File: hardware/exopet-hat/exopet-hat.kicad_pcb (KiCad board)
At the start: 2 copper layers, 65 x 56 mm, 48 parts, among them J1 BarrelJack_CUI_PJ-102AH_Horiz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, J10 TerminalBlock_Phoenix_MKDS-1,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, J11 TerminalBlock_Phoenix_MKDS-1,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, J2 SolderWire-1.5sqmm_1x02_P6mm_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, J3 PinSocket_2x20_P2.54mm_Vertic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, J4 Jack_3.5mm_CUI_SJ-3523-SMT_Ho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, J8 TerminalBlock_Phoenix_MKDS-1,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, J9 TerminalBlock_Phoenix_MKDS-1,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, K1 Relay_SPDT_Omron-G5LE-1, K2 Relay_SPDT_Omron-G5LE-1, K3 Relay_SPDT_Omron-G5LE-1, K4 Relay_SPDT_Omron-G5LE-1, Q1 TO-252-2, U2 SOIC-16_3.9x9.9mm_P1.27mm, U4 SOIC-8_3.9x4.9mm_P1.27mm, U5 D_SOD-323

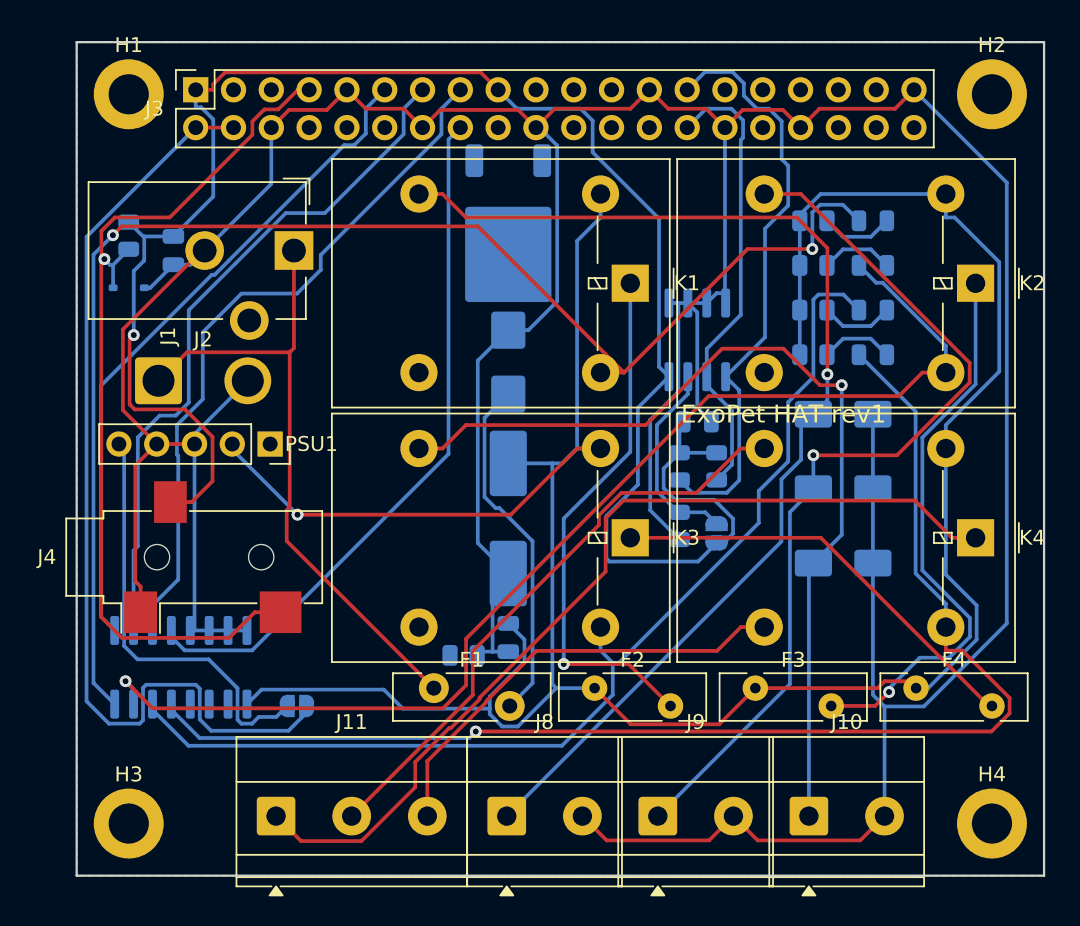
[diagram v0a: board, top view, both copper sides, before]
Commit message: Regroup HAT terminals per function; add float switch inputs
- Front edge: CH1/CH2/CH3 switched-12V blocks separated, CH4 dry
  contact last; left edge: FLOAT1, FLOAT2, TEMP sensor stack
- Temperature input is now a 3-pos screw terminal (TRS jack and JST
  both removed) - bare probe wires screw straight in
- Added the missing float switch inputs: GPIO16 (tank, matches hub
  code) and GPIO12 (sump spec), each with 10k pull-up, 1k series
  resistor, and 100nF filter
- All terminals now Phoenix PT-1,5 3.5mm; J2 aux 12V input removed
  (barrel jack sole input)
- Rerouted: 112 connections, 0 unrouted; DRC fully clean (0 violations)

Co-Authored-By: Claude Fable 5 <noreply@anthropic.com>
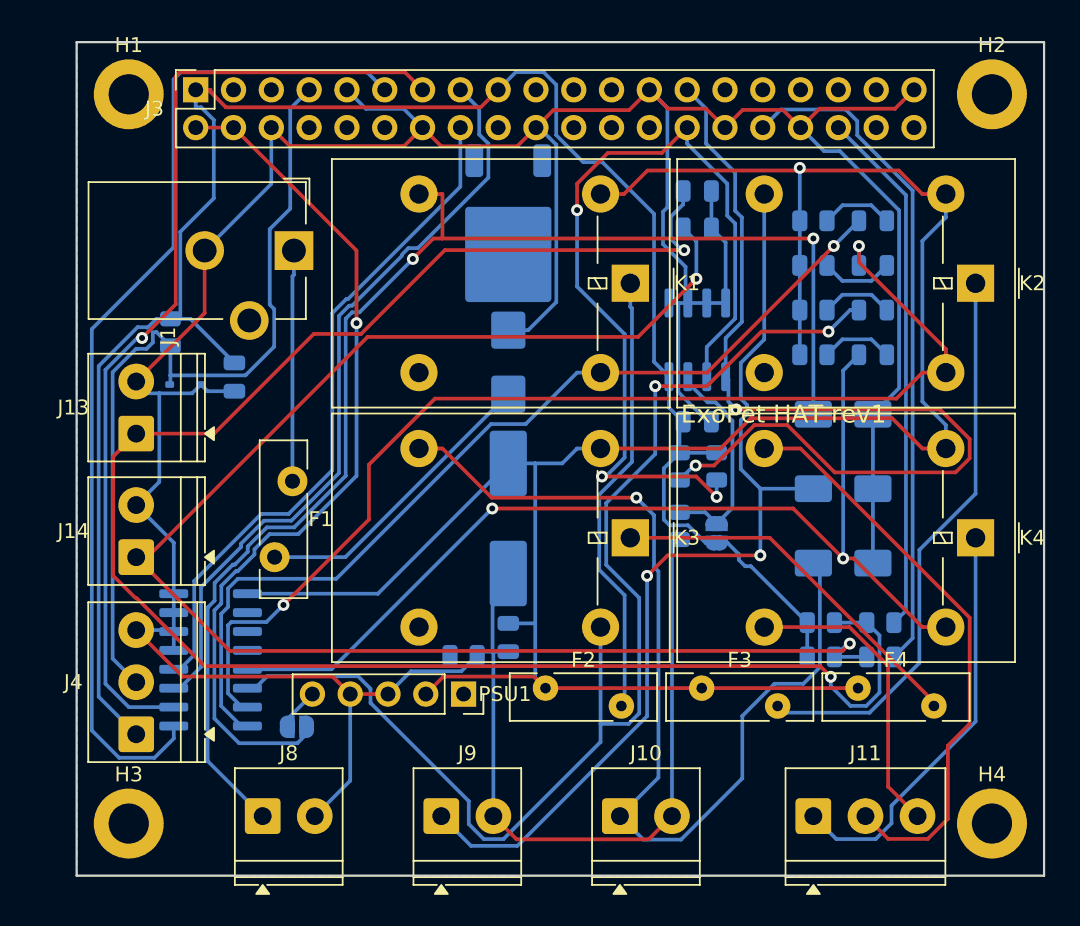
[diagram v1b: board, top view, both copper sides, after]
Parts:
- removed J2: SolderWire-1.5sqmm_1x02_P6mm_D1.7mm_OD3mm, Connector_Wire:SolderWire-1.5sqmm_1x02_P6mm_D1.7mm_OD3mm
- added C5: C_0805_2012Metric, Capacitor_SMD:C_0805_2012Metric, B.Cu at (41.7, 10.0)
- added C6: C_0805_2012Metric, Capacitor_SMD:C_0805_2012Metric, B.Cu at (41.7, 12.5)
- added J13: TerminalBlock_Phoenix_PT-1,5-2-3.5-H_1x02_P3.50mm_Horizontal, TerminalBlock_Phoenix:TerminalBlock_Phoenix_PT-1,5-2-3.5-H_1x02_P3.50mm_Horizontal, F.Cu at (4.00, 26.3)
- added J14: TerminalBlock_Phoenix_PT-1,5-2-3.5-H_1x02_P3.50mm_Horizontal, TerminalBlock_Phoenix:TerminalBlock_Phoenix_PT-1,5-2-3.5-H_1x02_P3.50mm_Horizontal, F.Cu at (4.00, 34.6)
- added R10: R_0805_2012Metric, Resistor_SMD:R_0805_2012Metric, B.Cu at (50.0, 39.0)
- added R11: R_0805_2012Metric, Resistor_SMD:R_0805_2012Metric, B.Cu at (50.0, 41.3)
- added R12: R_0805_2012Metric, Resistor_SMD:R_0805_2012Metric, B.Cu at (54.0, 39.0)
- added R13: R_0805_2012Metric, Resistor_SMD:R_0805_2012Metric, B.Cu at (54.0, 41.3)
- J10, J8, J9: value TerminalBlock_Phoenix_MKDS-1,5-2-5.08_1x02_P5.08mm_Horizontal -> TerminalBlock_Phoenix_PT-1,5-2-3.5-H_1x02_P3.50mm_Horizontal; footprint TerminalBlock_Phoenix:TerminalBlock_Phoenix_MKDS-1,5-2-5.08_1x02_P5.08mm_Horizontal -> TerminalBlock_Phoenix:TerminalBlock_Phoenix_PT-1,5-2-3.5-H_1x02_P3.50mm_Horizontal
- J11: value TerminalBlock_Phoenix_MKDS-1,5-3-5.08_1x03_P5.08mm_Horizontal -> TerminalBlock_Phoenix_PT-1,5-3-3.5-H_1x03_P3.50mm_Horizontal; footprint TerminalBlock_Phoenix:TerminalBlock_Phoenix_MKDS-1,5-3-5.08_1x03_P5.08mm_Horizontal -> TerminalBlock_Phoenix:TerminalBlock_Phoenix_PT-1,5-3-3.5-H_1x03_P3.50mm_Horizontal
- J4: value Jack_3.5mm_CUI_SJ-3523-SMT_Horizontal -> TerminalBlock_Phoenix_PT-1,5-3-3.5-H_1x03_P3.50mm_Horizontal; footprint Connector_Audio:Jack_3.5mm_CUI_SJ-3523-SMT_Horizontal -> TerminalBlock_Phoenix:TerminalBlock_Phoenix_PT-1,5-3-3.5-H_1x03_P3.50mm_Horizontal
- moved J11 36.1 mm to (49.5, 52.0)
- moved PSU1 21.2 mm to (26.0, 43.8)
- moved F1 16.8 mm to (14.5, 29.5), turned to -90 degrees
- moved J8 16.4 mm to (12.5, 52.0)
- moved J9 14.5 mm to (24.5, 52.0)
- moved J10 12.7 mm to (36.5, 52.0)
- moved J4 12.5 mm to (4.00, 46.5)
- moved C3 9.44 mm to (10.6, 22.5)
- moved U5 7.53 mm to (7.30, 23.0)
- moved R2 7.08 mm to (6.30, 19.5)
- moved F4 3.90 mm to (52.5, 43.4)
- moved F3 3.60 mm to (42.0, 43.4)
- moved F2 3.30 mm to (31.5, 43.4)
- moved U2 2.06 mm to (9.00, 41.5), turned to 0 degrees
- moved JP1 1.40 mm to (14.8, 46.0)
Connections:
- J3 pad 32: unconnected-(J3-PWM0/GPIO12-Pad32) -> FLOAT2_GPIO
- J3 pad 36: unconnected-(J3-GPIO16-Pad36) -> FLOAT1_GPIO
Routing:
- net FLOAT1_SW: track 0.00 -> 119.9 mm, vias 0 -> 2
- net FLOAT2_SW: track 0.00 -> 103.5 mm, vias 0 -> 2
- net FLOAT2_GPIO: track 0.00 -> 45.2 mm
- net FLOAT1_GPIO: track 0.00 -> 35.5 mm
- net CH4_COM: track 61.4 -> 27.8 mm
- net RLY1_DRV: track 95.2 -> 63.0 mm, vias 2 -> 1
- net +12V: track 184.9 -> 155.3 mm
- net EEPROM_SCL: track 30.9 -> 59.0 mm, vias 0 -> 3
- net +12V_IN: track 43.3 -> 15.5 mm
- net +5V_BUCK: track 28.6 -> 2.90 mm
- net GND: track 302.2 -> 277.2 mm
- net EEPROM_SDA: track 39.8 -> 64.3 mm, vias 0 -> 2
- net GPIO17: track 45.1 -> 68.5 mm
- net GPIO27: track 46.5 -> 65.4 mm, vias 0 -> 1
- net RLY4_DRV: track 87.1 -> 68.8 mm, vias 1 -> 2
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
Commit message: Fix GPIO socket to bottom side per official HAT template; refresh fab package
Critical fix caught before ordering: the 2x20 socket body was generated
on the top side and off-position — physically unable to mate with a Pi.
Now matches KiCad's official RaspberryPi-HAT template exactly (B.Cu,
pin 1 at 8.37,4.77 from the hole datum) with tools/verify_j3.py as a
permanent regression assert.

Also: C1 changed to low-profile 6.3x7.7mm (330uF) for under-HAT
clearance; verified in-stock LCSC codes baked into the assembly BOM
(PC104 stacking socket C35165, CUI PJ-102A C20518877, KF350 terminals,
RGEF500/RXEF110 fuses, PESD5V0S1BA ESD diode, 1x5 socket C50950).
Rerouted, DRC clean (0 errors), renders and fab files regenerated.

Co-Authored-By: Claude Fable 5 <noreply@anthropic.com>
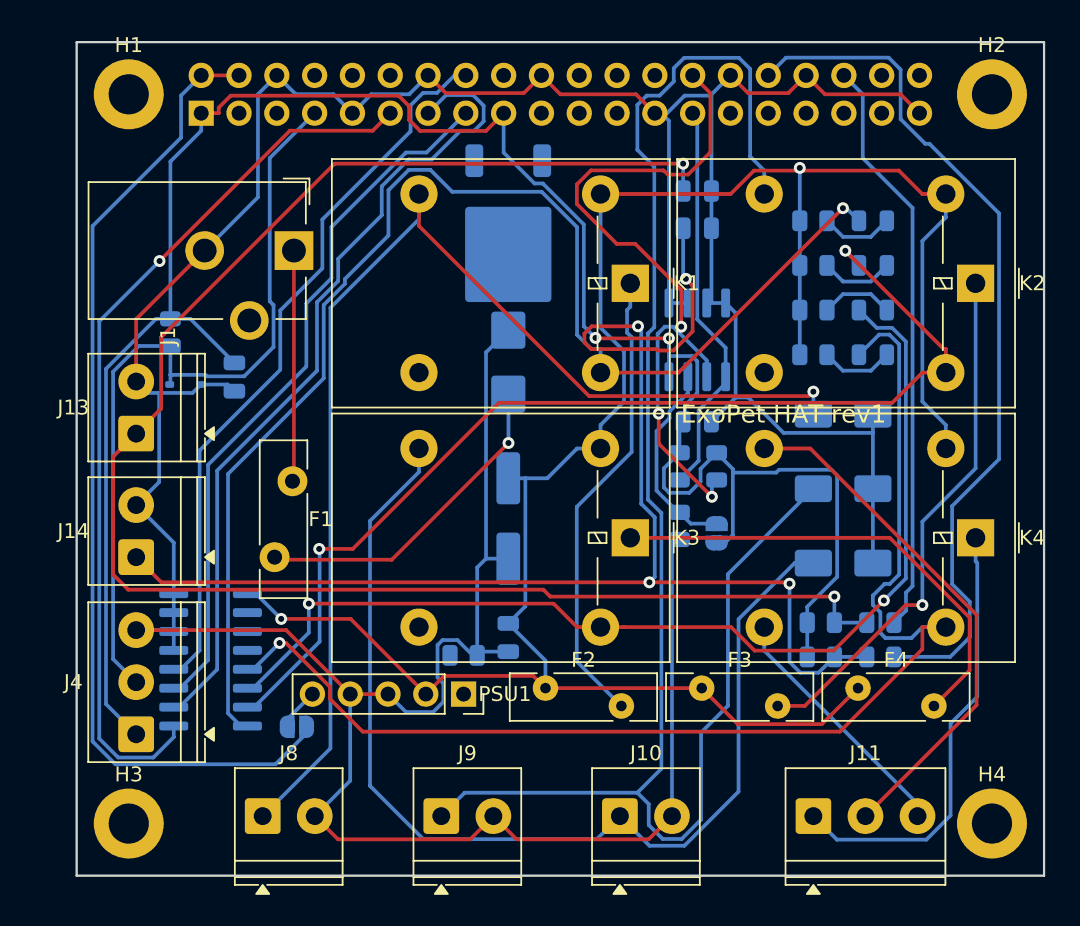
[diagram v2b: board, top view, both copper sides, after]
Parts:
- C1: value CP_Elec_8x10.5 -> CP_Elec_6.3x7.7; footprint Capacitor_SMD:CP_Elec_8x10.5 -> Capacitor_SMD:CP_Elec_6.3x7.7
- J3: moved to B.Cu
- moved J3 1.61 mm to (8.37, 4.77), turned to -90 degrees
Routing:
- net CH2_OUT: track 65.3 -> 112.5 mm, vias 2 -> 0
- net EEPROM_SDA: track 64.3 -> 26.8 mm, vias 2 -> 0
- net RLY1_DRV: track 63.0 -> 89.2 mm
- net RLY4_DRV: track 68.8 -> 83.3 mm, vias 2 -> 1
- net FLOAT2_GPIO: track 45.2 -> 58.2 mm
- net RLY3_DRV: track 83.4 -> 71.0 mm
- net +3V3: track 132.1 -> 144.1 mm, vias 0 -> 2
- net +12V: track 155.3 -> 143.4 mm, vias 1 -> 2
- net EEPROM_SCL: track 59.0 -> 48.6 mm
- net FLOAT2_SW: track 103.5 -> 93.3 mm, vias 2 -> 4
- net GPIO27: track 65.4 -> 55.2 mm, vias 1 -> 0
- net CH1_OUT: track 90.0 -> 81.2 mm, vias 2 -> 1
- net GPIO17: track 68.5 -> 60.2 mm, vias 0 -> 1
- net +5V: track 58.4 -> 66.6 mm, vias 1 -> 0
- net FLOAT1_SW: track 119.9 -> 112.0 mm
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
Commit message: HAT rev 2: schematic + placement — integrated buck, D1 fix, top LEDs, TPs
TPS54302 synchronous buck replaces the Pololu socket (datasheet-derived
5.06V design; 5A TPS54531 didn't fit the relay-pad corridors). D1 nets
corrected + bidirectional SMBJ16CA. Channel LEDs move to the top
between terminal blocks; 12V/5V rail LEDs + 4 test points top-left.
Terminal +/- and COM/NO/NC silk, jack polarity text, PTC fuse drills
enlarged to 1.1mm. New check_polarity.py lints every polarized part
from the netlist; check_placement.py now also catches SMD-vs-THT-pad
collisions (found two latent rev-1 near-misses). ERC clean, polarity
lint clean, placement clean, J3 template-verified.

Co-Authored-By: Claude Fable 5 <noreply@anthropic.com>
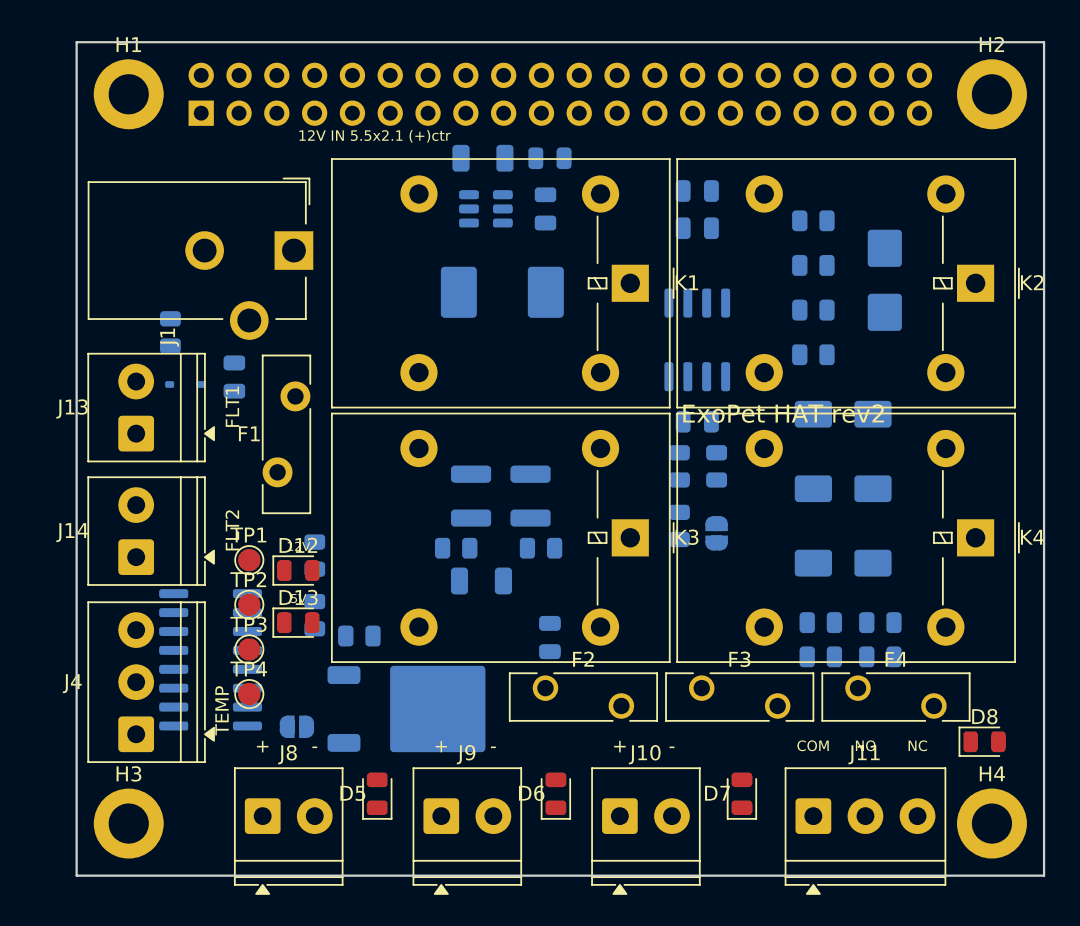
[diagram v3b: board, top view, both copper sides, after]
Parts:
- removed C1: CP_Elec_6.3x7.7, Capacitor_SMD:CP_Elec_6.3x7.7
- removed PSU1: PinSocket_1x05_P2.54mm_Vertical, Connector_PinSocket_2.54mm:PinSocket_1x05_P2.54mm_Vertical
- added C10: C_0805_2012Metric, Capacitor_SMD:C_0805_2012Metric, B.Cu at (31.8, 7.80)
- added C11: C_1210_3225Metric, Capacitor_SMD:C_1210_3225Metric, B.Cu at (26.5, 30.5)
- added C12: C_1210_3225Metric, Capacitor_SMD:C_1210_3225Metric, B.Cu at (30.5, 30.5)
- added C16: C_1206_3216Metric, Capacitor_SMD:C_1206_3216Metric, B.Cu at (27.2, 36.2)
- added C7: C_0805_2012Metric, Capacitor_SMD:C_0805_2012Metric, B.Cu at (31.5, 11.2)
- added C8: C_1206_3216Metric, Capacitor_SMD:C_1206_3216Metric, B.Cu at (27.3, 7.80)
- added D12: LED_0805_2012Metric, LED_SMD:LED_0805_2012Metric, F.Cu at (14.9, 35.5)
- added D13: LED_0805_2012Metric, LED_SMD:LED_0805_2012Metric, F.Cu at (14.9, 39.0)
- added L1: L_Vishay_IHLP-2525, Inductor_SMD:L_Vishay_IHLP-2525, B.Cu at (28.6, 16.8)
- added R16: R_0805_2012Metric, Resistor_SMD:R_0805_2012Metric, B.Cu at (25.5, 34.0)
- added R17: R_0805_2012Metric, Resistor_SMD:R_0805_2012Metric, B.Cu at (31.2, 34.0)
- added R19: R_0805_2012Metric, Resistor_SMD:R_0805_2012Metric, B.Cu at (16.0, 34.5)
- added R20: R_0805_2012Metric, Resistor_SMD:R_0805_2012Metric, B.Cu at (16.0, 38.5)
- added TP1: TestPoint_Pad_D1.5mm, TestPoint:TestPoint_Pad_D1.5mm, F.Cu at (11.6, 34.8)
- added TP2: TestPoint_Pad_D1.5mm, TestPoint:TestPoint_Pad_D1.5mm, F.Cu at (11.6, 37.8)
- added TP3: TestPoint_Pad_D1.5mm, TestPoint:TestPoint_Pad_D1.5mm, F.Cu at (11.6, 40.8)
- added TP4: TestPoint_Pad_D1.5mm, TestPoint:TestPoint_Pad_D1.5mm, F.Cu at (11.6, 43.8)
- added U6: SOT-23-6, Package_TO_SOT_SMD:SOT-23-6, B.Cu at (27.5, 11.2)
- D5, D6, D7, D8: moved to F.Cu
- moved D5 50.9 mm to (20.2, 50.5), turned to 90 degrees
- moved D6 41.4 mm to (32.2, 50.5), turned to 90 degrees
- moved D7 33.7 mm to (44.7, 50.5), turned to 90 degrees
- moved Q1 32.4 mm to (23.0, 44.8), turned to 0 degrees
- moved D8 27.1 mm to (61.0, 47.0)
- moved D1 25.9 mm to (54.3, 16.0)
- moved R1 7.12 mm to (19.0, 39.9)
- moved C2 2.80 mm to (31.8, 40.0)
- moved F1 1.17 mm to (13.5, 28.9), turned to 90 degrees
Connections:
- D1 pad 1: GND -> +12V_F
- D1 pad 2: +12V_F -> GND
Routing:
- net GND: track 273.5 -> 0.00 mm
- net +3V3: track 144.1 -> 0.00 mm, vias 2 -> 0
- net +12V: track 143.4 -> 0.00 mm, vias 2 -> 0
- net CH2_OUT: track 112.5 -> 0.00 mm
- net FLOAT1_SW: track 112.0 -> 0.00 mm, vias 2 -> 0
- net FLOAT2_SW: track 93.3 -> 0.00 mm, vias 4 -> 0
- net RLY1_DRV: track 89.2 -> 0.00 mm, vias 1 -> 0
- net RLY4_DRV: track 83.3 -> 0.00 mm, vias 1 -> 0
- net CH1_OUT: track 81.2 -> 0.00 mm, vias 1 -> 0
- net RLY2_DRV: track 72.2 -> 0.00 mm, vias 2 -> 0
- net CH3_OUT: track 71.4 -> 0.00 mm
- net RLY3_DRV: track 71.0 -> 0.00 mm, vias 2 -> 0
- net +5V: track 66.6 -> 0.00 mm
- net GPIO17: track 60.2 -> 0.00 mm, vias 1 -> 0
- net FLOAT2_GPIO: track 58.2 -> 0.00 mm
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- removed copper zone on B.Cu, net GND
- removed copper zone on F.Cu, net GND
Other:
- board text added: "+"
- board text added: "-"
- board text added: "12V"
- board text added: "12V IN 5.5x2.1 (+)ctr"
- board text added: "5V"
- board text added: "COM"
- board text added: "ExoPet HAT rev2"
- board text added: "FLT1"
- board text added: "FLT2"
- board text added: "NC"
- board text added: "NO"
- board text added: "TEMP"
- board text removed: "ExoPet HAT rev1"

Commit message: HAT rev 2: routed board, DRC clean, renders
Locked pre-placed +3V3 bridge (J3.17->C4.1) works around freerouting's
persistent stranding of that island; router completes the rest. Zones
re-added post-route; 0 DRC violations, 0 unconnected. J3 template
check, placement checker (with THT-pad awareness), and polarity lint
all pass. Top/bottom renders regenerated.

Co-Authored-By: Claude Fable 5 <noreply@anthropic.com>
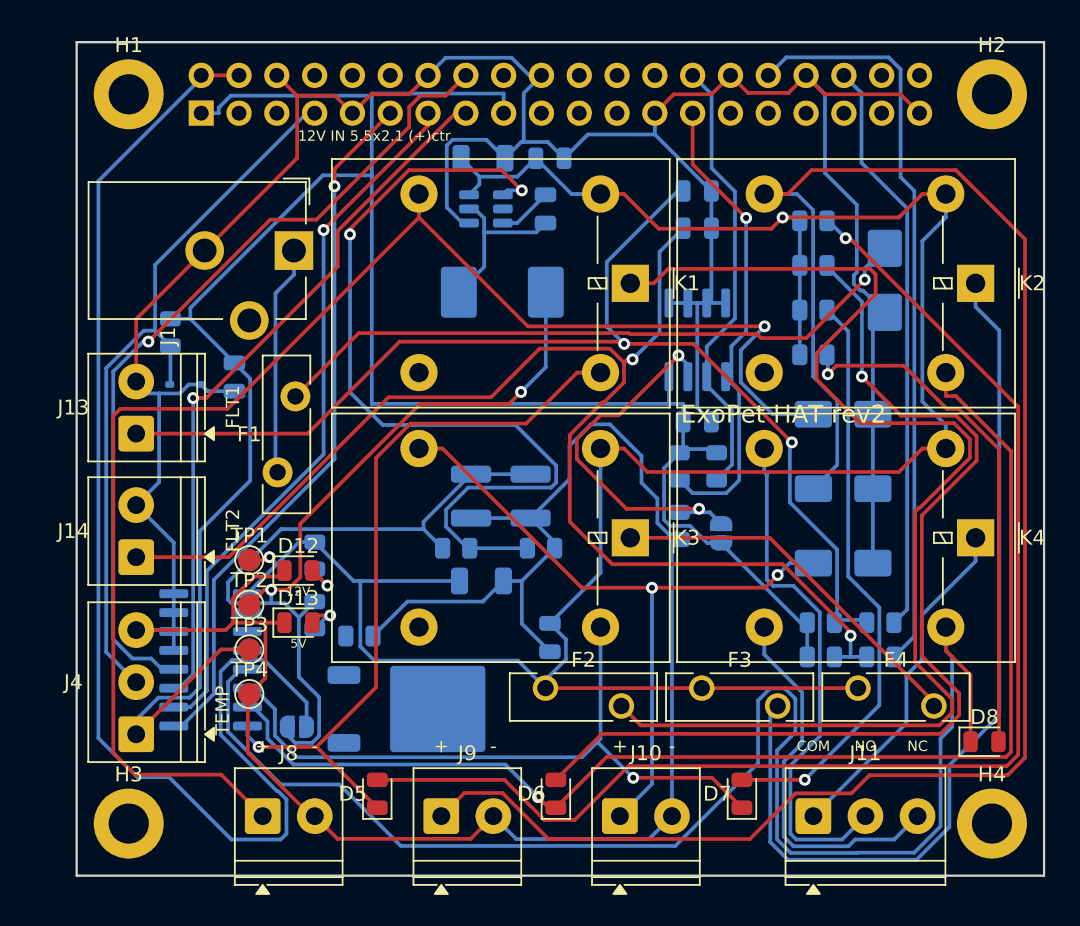
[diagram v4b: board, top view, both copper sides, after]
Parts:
- moved JP2 0.30 mm to (43.3, 33.0)
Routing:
- net GND: track 0.00 -> 306.0 mm
- net +12V: track 0.00 -> 167.4 mm, vias 0 -> 2
- net +3V3: track 0.00 -> 153.3 mm
- net CH2_OUT: track 0.00 -> 122.1 mm
- net CH1_OUT: track 0.00 -> 98.5 mm, vias 0 -> 1
- net RLY4_DRV: track 0.00 -> 97.8 mm
- net FLOAT2_SW: track 0.00 -> 87.9 mm, vias 0 -> 2
- net LED1_A: track 0.00 -> 87.3 mm, vias 0 -> 1
- net +5V: track 0.00 -> 87.2 mm
- net RLY2_DRV: track 0.00 -> 84.0 mm, vias 0 -> 1
- net CH1_FUSED: track 0.00 -> 81.7 mm
- net +5V_BUCK: track 0.00 -> 79.6 mm, vias 0 -> 2
- net FLOAT1_SW: track 0.00 -> 78.1 mm, vias 0 -> 2
- net LED2_A: track 0.00 -> 67.9 mm, vias 0 -> 1
- net CH2_FUSED: track 0.00 -> 61.4 mm
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- added copper zone on B.Cu, net GND
- added copper zone on F.Cu, net GND
